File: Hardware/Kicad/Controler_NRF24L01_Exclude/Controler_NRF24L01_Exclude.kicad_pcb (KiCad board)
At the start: 2 copper layers, 73 parts, among them J1 Conn_01x02, J2 Conn_02x07_Odd_Even, SW1 SW_DIP_x01, SW10 SW_DIP_x01, SW11 SW_Push, SW12 SW_Push, SW13 SW_Push, SW2 SW_Push, SW3 SW_Push, SW4 SW_Push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

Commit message: Exculde finish
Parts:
- added D19: D_Small, LED_SMD:LED_0603_1608Metric_Pad1.05x0.95mm_HandSolder, F.Cu at (129.0, 105.0)
- J1: moved to B.Cu
- SW11, SW12, SW13, SW2, SW3, SW4, SW5, SW6, SW8, SW9: footprint Button_Switch_THT:SW_PUSH_6mm_H5mm -> Button_Switch_SMD:SW_SPST_B3S-1000
- moved R21 156.6 mm to (114.0, 63.5), turned to -90 degrees
- moved R22 152.5 mm to (117.6, 63.4), turned to -90 degrees
- moved R20 151.7 mm to (110.5, 63.5), turned to -90 degrees
- moved R1 134.5 mm to (121.8, 80.7)
- moved R23 121.1 mm to (149.4, 62.3), turned to 90 degrees
- moved R24 118.9 mm to (150.9, 62.3), turned to 90 degrees
- moved R29 118.5 mm to (158.4, 62.3), turned to 90 degrees
- moved R25 116.7 mm to (152.4, 62.3), turned to 90 degrees
- moved R30 116.1 mm to (159.9, 62.3), turned to 90 degrees
- moved R26 114.5 mm to (153.9, 62.3), turned to 90 degrees
- moved R31 113.9 mm to (161.4, 62.3), turned to 90 degrees
- moved R27 112.4 mm to (155.4, 62.3), turned to 90 degrees
- moved R32 111.6 mm to (162.9, 62.3), turned to 90 degrees
- moved R28 110.3 mm to (156.9, 62.3), turned to 90 degrees
- moved R11 110.1 mm to (159.7, 71.8)
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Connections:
- J1 pad 1: +3V8 -> Li-ion
- U1 pad 1: Glob_Alim -> Net-(D19-K)
- U1 pad 10: UC_Button -> Order_Search
- U1 pad 11: DC_Button -> Pin_Clock
- U1 pad 12: LC_Button -> Digital_Out_Put
- U1 pad 13: RC_Button -> MOSI
- U1 pad 14: unconnected-(U1-PB0-Pad14) -> DC_Button
- U1 pad 15: NES/SNES_switcher -> UC_Button
- U1 pad 17: Glob_Alim -> Net-(D19-K)
- U1 pad 2: Y_Button -> RC_Button
- U1 pad 20: Order_Search -> X_Button
- U1 pad 22: LED_Order -> Y_Button
- U1 pad 26: Pin_Clock -> DIODE_CLK
- U1 pad 27: Digital_Out_Put -> POWER_CHECK
- U1 pad 28: MOSI -> DIODE_SDA
- U1 pad 29: unconnected-(U1-PB6-Pad29) -> R
- U1 pad 3: X_Button -> LC_Button
- U1 pad 30: unconnected-(U1-PB7-Pad30) -> L
- U1 pad 31: unconnected-(U1-PH3-Pad31) -> NES/SNES_switcher
- U1 pad 4: NRST -> Reset_Buton 
- U1 pad 5: Glob_Alim -> Net-(D19-K)
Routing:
- net GND: track 0.00 -> 388.7 mm, vias 0 -> 54
- net Glob_Alim: track 0.00 -> 178.1 mm, vias 0 -> 9
- net DC_Button: track 0.00 -> 143.4 mm, vias 0 -> 2
- net L: track 0.00 -> 116.9 mm, vias 0 -> 8
- net POWER_CHECK: track 0.00 -> 108.7 mm
- net A_Button: track 0.00 -> 96.6 mm, vias 0 -> 6
- net B_Button: track 0.00 -> 78.6 mm, vias 0 -> 4
- net Order_Search: track 0.00 -> 75.5 mm, vias 0 -> 4
- net UC_Button: track 0.00 -> 72.9 mm, vias 0 -> 4
- net MOSI: track 0.00 -> 72.6 mm, vias 0 -> 4
- net X_Button: track 0.00 -> 71.6 mm, vias 0 -> 2
- net RC_Button: track 0.00 -> 71.2 mm, vias 0 -> 2
- net Y_Button: track 0.00 -> 62.4 mm, vias 0 -> 2
- net Net-(D19-K): track 0.00 -> 58.3 mm, vias 0 -> 3
- net DIODE_SDA: track 0.00 -> 57.9 mm, vias 0 -> 4
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- added copper zone on B.Cu, net (none)
- added copper zone on B.Cu, net GND
- added copper zone on F.Cu, net GND

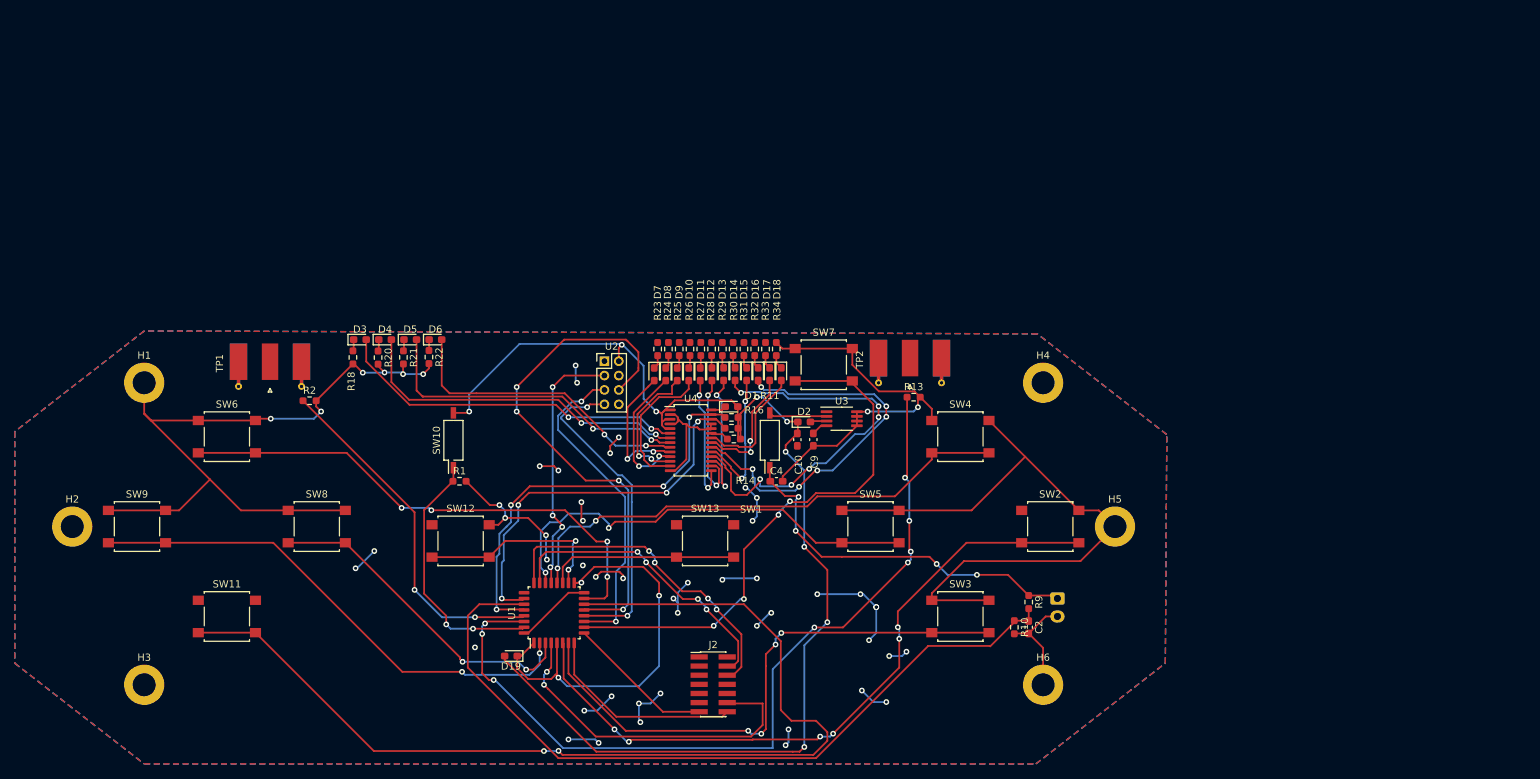
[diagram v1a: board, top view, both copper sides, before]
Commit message: update of the folder 'controler_NRF24L01_Exclude' -> replace by the correction given
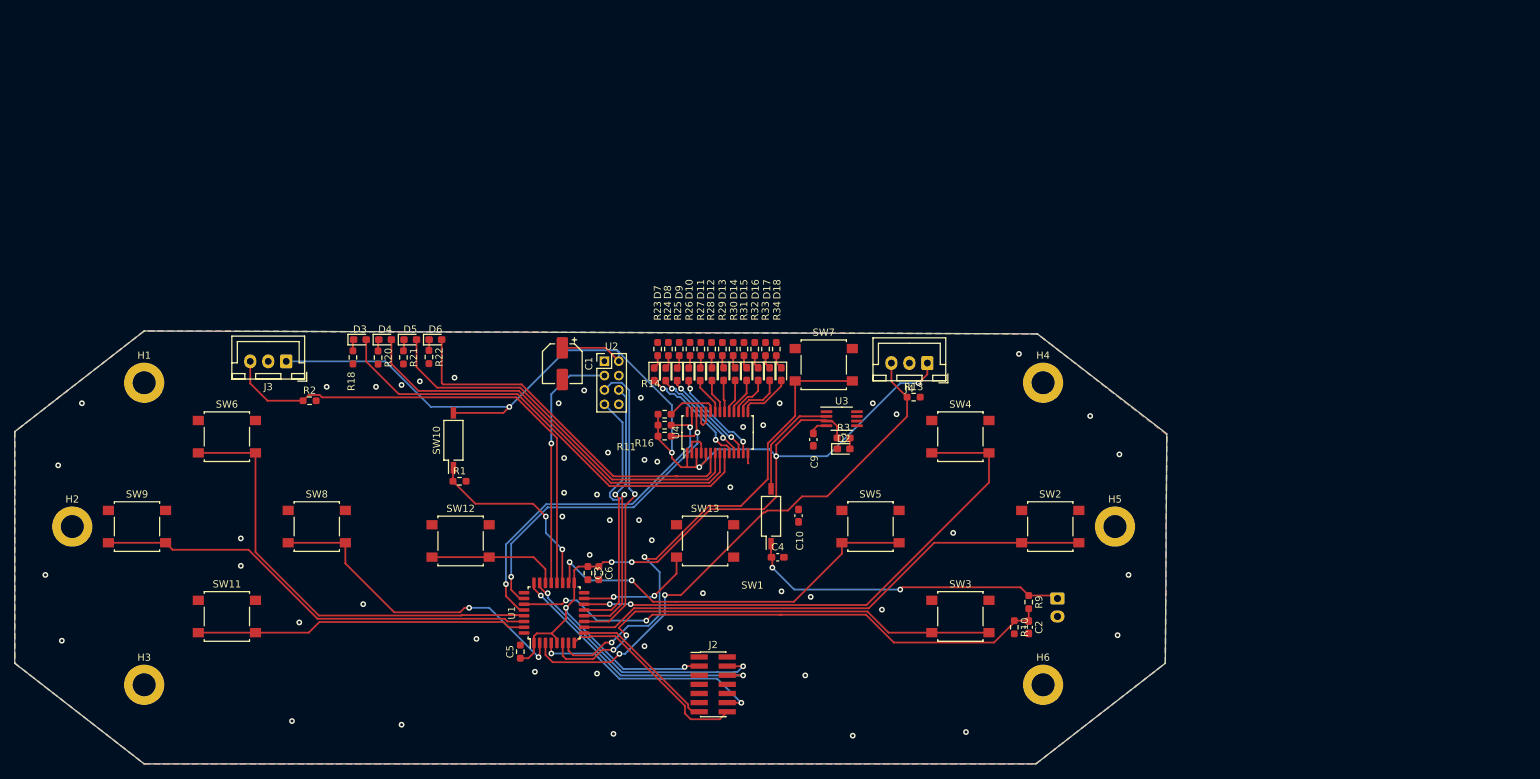
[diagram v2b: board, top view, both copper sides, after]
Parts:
- removed D1, D19: D_Small, LED_SMD:LED_0603_1608Metric_Pad1.05x0.95mm_HandSolder
- removed TP1: R, Connector_Coaxial:SMA_Molex_73251-1153_EdgeMount_Horizontal
- removed TP2: L, Connector_Coaxial:SMA_Molex_73251-1153_EdgeMount_Horizontal
- added C1: 100uF, Capacitor_SMD:CP_Elec_5x5.4, F.Cu at (136.1, 64.3)
- added C3: 100n, Resistor_SMD:R_0603_1608Metric_Pad0.98x0.95mm_HandSolder, F.Cu at (139.7, 93.5)
- added C5: 100n, Resistor_SMD:R_0603_1608Metric_Pad0.98x0.95mm_HandSolder, F.Cu at (130.3, 104.4)
- added C6: 10u, Resistor_SMD:R_0603_1608Metric_Pad0.98x0.95mm_HandSolder, F.Cu at (141.2, 93.5)
- added J3: Conn_01x03, Connector_JST:JST_XH_B3B-XH-A_1x03_P2.50mm_Vertical, F.Cu at (97.8, 64.0)
- added J4: Conn_01x03, Connector_JST:JST_XH_B3B-XH-A_1x03_P2.50mm_Vertical, F.Cu at (186.9, 64.3)
- added R3: R_Small, Resistor_SMD:R_0603_1608Metric_Pad0.98x0.95mm_HandSolder, F.Cu at (175.3, 74.7)
- moved C10 10.6 mm to (169.0, 85.5)
- moved C4 10.6 mm to (166.1, 91.3)
- moved SW1 10.6 mm to (165.2, 85.6)
- moved R16 10.2 mm to (150.4, 71.4), turned to 180 degrees
- moved R14 9.37 mm to (150.4, 74.4), turned to 0 degrees
- moved R11 9.37 mm to (150.4, 72.9), turned to 180 degrees
- moved D2 6.64 mm to (175.3, 76.2)
- moved U4 3.89 mm to (157.7, 73.9), turned to 90 degrees
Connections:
- D2 pad 1: Glob_Alim -> GND
- J2 pad 3: +3.3V -> Glob_Alim
- U1 pad 1: Net-(D19-K) -> Glob_Alim
- U1 pad 10: Order_Search -> A_Button
- U1 pad 14: DC_Button -> X_Button
- U1 pad 15: UC_Button -> SE_Button
- U1 pad 17: Net-(D19-K) -> Glob_Alim
- U1 pad 18: ST_Button -> Y_Button
- U1 pad 19: SE_Button -> NES/SNES_switcher
- U1 pad 2: RC_Button -> LC_Button
- U1 pad 20: X_Button -> R
- U1 pad 22: Y_Button -> ST_Button
- U1 pad 29: R -> UC_Button
- U1 pad 3: LC_Button -> L
- U1 pad 30: L -> RC_Button
- U1 pad 31: NES/SNES_switcher -> DC_Button
- U1 pad 5: Net-(D19-K) -> Glob_Alim
- U1 pad 6: A_Button -> B_Button
- U1 pad 7: B_Button -> Order_Search
- U3 pad 3: Net-(D2-A) -> Glob_Alim
- U4 pad 15: Net-(D11-A) -> Net-(D18-A)
- U4 pad 16: Net-(D12-A) -> Net-(D17-A)
- U4 pad 17: Net-(D13-A) -> Net-(D16-A)
- U4 pad 18: Net-(D14-A) -> Net-(D15-A)
- U4 pad 19: Net-(D15-A) -> Net-(D14-A)
- U4 pad 20: Net-(D16-A) -> Net-(D13-A)
- U4 pad 21: Net-(D17-A) -> Net-(D12-A)
- U4 pad 22: Net-(D18-A) -> Net-(D11-A)
- U4 pad 28: Net-(D1-K) -> Glob_Alim
- U4 pad 6: Net-(D3-A) -> Net-(D6-A)
- U4 pad 7: Net-(D4-A) -> Net-(D5-A)
- U4 pad 8: Net-(D5-A) -> Net-(D4-A)
- U4 pad 9: Net-(D6-A) -> Net-(D3-A)
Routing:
- net GND: track 388.7 -> 9.77 mm
- net DC_Button: track 143.4 -> 46.2 mm, vias 2 -> 0
- net Glob_Alim: track 178.1 -> 237.4 mm
- net Net-(D19-K): track 58.3 -> 0.00 mm, vias 3 -> 0
- net Net-(D14-A): track 57.1 -> 4.71 mm, vias 6 -> 0
- net Net-(D16-A): track 53.3 -> 5.87 mm, vias 6 -> 0
- net L: track 116.9 -> 76.4 mm, vias 8 -> 2
- net MOSI: track 72.6 -> 36.1 mm, vias 4 -> 1
- net POWER_CHECK: track 108.7 -> 76.9 mm, vias 0 -> 2
- net A_Button: track 96.6 -> 73.8 mm, vias 6 -> 0
- net R: track 49.6 -> 69.7 mm, vias 2 -> 0
- net Net-(D13-A): track 20.3 -> 4.43 mm, vias 2 -> 0
- net Reset_Buton : track 48.3 -> 32.7 mm
- net Net-(D15-A): track 19.8 -> 5.11 mm, vias 2 -> 0
- net Net-(D12-A): track 19.0 -> 4.82 mm, vias 2 -> 0
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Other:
- board outline added: 160.2 x 60.2 mm

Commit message: Update v2.2a - Plug_NRF24L01_Exclude (SWD_Connector, GND Vias) - Controller_NRF24L01_Exclude (Schematic) - Cleaned Folders
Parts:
- added C7: 100µF, Capacitor_SMD:C_0603_1608Metric_Pad1.08x0.95mm_HandSolder, F.Cu at (138.0, 90.2)
- added R4: 10k, Resistor_SMD:R_0603_1608Metric_Pad0.98x0.95mm_HandSolder, F.Cu at (142.4, 88.9)
- added R5: 1K, Resistor_SMD:R_0603_1608Metric_Pad0.98x0.95mm_HandSolder, F.Cu at (130.2, 54.4)
- added R6: 1K, Resistor_SMD:R_0603_1608Metric_Pad0.98x0.95mm_HandSolder, F.Cu at (124.5, 54.4)
- added U5: PCF8574TS, Package_SO:SSOP-20_4.4x6.5mm_P0.65mm, F.Cu at (136.1, 84.9)
- C1: footprint Capacitor_SMD:CP_Elec_5x5.4 -> Capacitor_SMD:C_0603_1608Metric_Pad1.08x0.95mm_HandSolder; moved to B.Cu
- C3, C5, C6: footprint Resistor_SMD:R_0603_1608Metric_Pad0.98x0.95mm_HandSolder -> Capacitor_SMD:C_0603_1608Metric_Pad1.08x0.95mm_HandSolder
- R3: value R_Small -> 1K
- U2: footprint Connector_PinHeader_2.00mm:PinHeader_2x04_P2.00mm_Vertical -> Connector_PinHeader_2.54mm:PinHeader_2x04_P2.54mm_Vertical
- moved J1 30.8 mm to (176.4, 108.4)
- moved C2 29.8 mm to (173.4, 112.3)
- moved R10 29.8 mm to (171.4, 112.3)
- moved R9 29.8 mm to (173.4, 108.8)
- moved C1 3.36 mm to (138.4, 61.9)
- moved U2 1.95 mm to (142.2, 62.1)
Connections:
- U1 pad 18: Y_Button -> GPIO_EX_CLK
- U1 pad 22: ST_Button -> GPIO_EX_SERIAL_DATA
- U1 pad 25: unconnected-(U1-PA15-Pad25) -> CSN_nRF24
- U2 pad 4: unconnected-(U2-CSN-Pad4) -> CSN_nRF24
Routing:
- net CSN_nRF24: track 0.00 -> 69.3 mm, vias 0 -> 1
- net POWER_CHECK: track 76.9 -> 52.7 mm
- net DIODE_OE: track 7.14 -> 28.8 mm, vias 0 -> 2
- net Li-ion: track 45.1 -> 25.1 mm
- net GND: track 9.77 -> 27.2 mm, vias 54 -> 60
- net Glob_Alim: track 237.4 -> 252.5 mm, vias 9 -> 12
- net SE_Button: track 16.6 -> 29.6 mm, vias 2 -> 4
- net ST_Button: track 18.4 -> 30.4 mm, vias 0 -> 2
- net GPIO_EX_CLK: track 0.00 -> 8.79 mm, vias 0 -> 2
- net GPIO_EX_SERIAL_DATA: track 0.00 -> 7.89 mm, vias 0 -> 2
- net RX/TX: track 34.7 -> 39.6 mm
- net R: track 69.7 -> 73.4 mm
- net Net-(C7-Pad1): track 0.00 -> 3.70 mm
- net Pin_Clock: track 41.7 -> 43.5 mm
- net Y_Button: track 55.3 -> 53.6 mm
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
